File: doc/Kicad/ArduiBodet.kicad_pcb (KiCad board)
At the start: 2 copper layers, 80 x 49.5 mm, 15 parts, among them CON1 BARREL_JACK, IC1 ATMEGA328-P, IC2 SN754410, P1 ISP10PIN, P2 DS3231_Breakout_Connector, P3 Moteur Horloge, SW1 SWITCH_INV, SW2 Switch_DPST

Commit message: routing in progress
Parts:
- added C4: 1000 uF, Capacitors_Elko_ThroughHole:Elko_vert_20x10mm_RM2.5, F.Cu at (157.5, 95.2)
- added C5: 330nF, Capacitors_ThroughHole:C_Rect_L4_W2.5_P2.5, F.Cu at (167.6, 95.2)
- added U1: LM7805CT, Power_Integrations:TO-220, F.Cu at (146.1, 102.9)
- C2: value CP -> 100 nF; footprint Capacitors_Elko_ThroughHole:Elko_vert_20x10mm_RM2.5 -> Capacitors_ThroughHole:C_Rect_L4_W2.5_P2.5
- CON1: footprint Connect:BARREL_JACK -> myLib:BARREL_JACK_FR
- moved C2 50.8 mm to (143.5, 95.2), turned to 0 degrees
- moved C1 18.5 mm to (186.7, 113.0)
- moved SW1 15.9 mm to (177.8, 109.2)
- moved P2 14.9 mm to (129.5, 115.6)
- moved IC2 13.7 mm to (188.0, 128.3)
- moved R2 13.7 mm to (176.5, 132.1)
- moved IC1 13.7 mm to (160.0, 120.7)
- moved P3 13.7 mm to (171.4, 138.4)
- moved SW2 13.7 mm to (153.7, 134.6)
- moved C3 13.7 mm to (158.8, 129.5)
- moved R3 13.7 mm to (156.2, 144.8)
- moved D1 13.7 mm to (161.3, 139.7)
- moved P1 13.5 mm to (158.8, 105.4)
- moved R1 11.7 mm to (134.6, 119.4)
- moved CON1 2.84 mm to (190.5, 97.8)
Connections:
- CON1 pad 2: GNDA -> Net-(CON1-Pad2)
- CON1 pad 3: Net-(CON1-Pad3) -> GNDA
- IC2 pad 8: Net-(C1-Pad1) -> Net-(C4-Pad1)
- SW1 pad 1: Net-(C1-Pad1) -> Net-(SW1-Pad1)
- SW1 pad 3: Net-(SW1-Pad3) -> Net-(C4-Pad1)
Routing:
- net GNDA: track 0.00 -> 143.9 mm
- net Net-(C4-Pad1): track 0.00 -> 130.0 mm
- net Net-(C1-Pad1): track 0.00 -> 76.2 mm
- net Net-(IC2-Pad3): track 0.00 -> 62.8 mm
- net Net-(IC1-Pad1): track 0.00 -> 52.1 mm, vias 0 -> 2
- net Net-(IC1-Pad16): track 0.00 -> 27.5 mm
- net Net-(IC1-Pad4): track 0.00 -> 25.0 mm
- net Net-(IC1-Pad17): track 0.00 -> 24.1 mm, vias 0 -> 2
- net Net-(IC1-Pad27): track 0.00 -> 20.9 mm
- net Net-(IC1-Pad28): track 0.00 -> 16.6 mm
- net Net-(CON1-Pad1): track 0.00 -> 11.6 mm
- net Net-(IC1-Pad19): track 0.00 -> 11.4 mm
- net Net-(IC1-Pad18): track 0.00 -> 11.4 mm
- net Net-(IC1-Pad6): track 0.00 -> 11.2 mm
- net Net-(R3-Pad2): track 0.00 -> 7.62 mm
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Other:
- board size 80 x 49.5 mm -> 80 x 61 mm

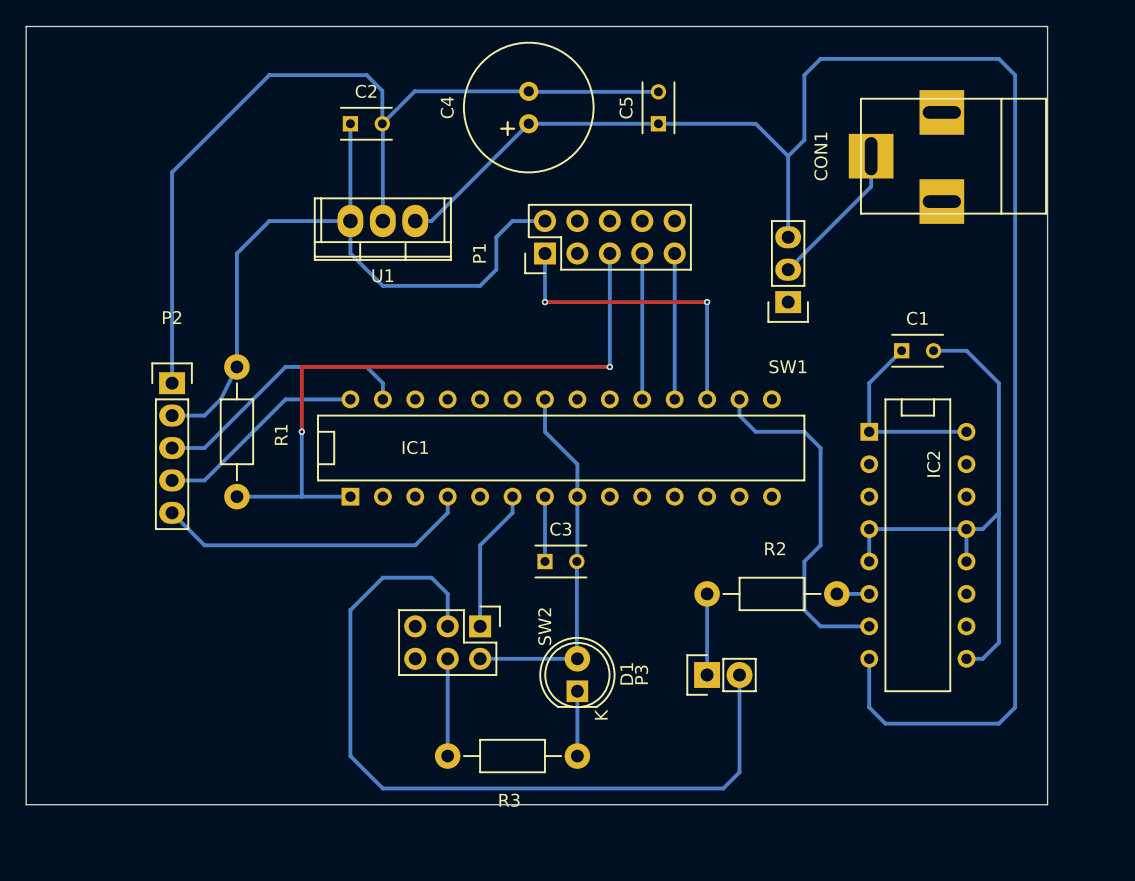
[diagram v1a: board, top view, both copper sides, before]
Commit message: fully routed #1 fixed custom BARREL_JACK_FR.kicad_mod
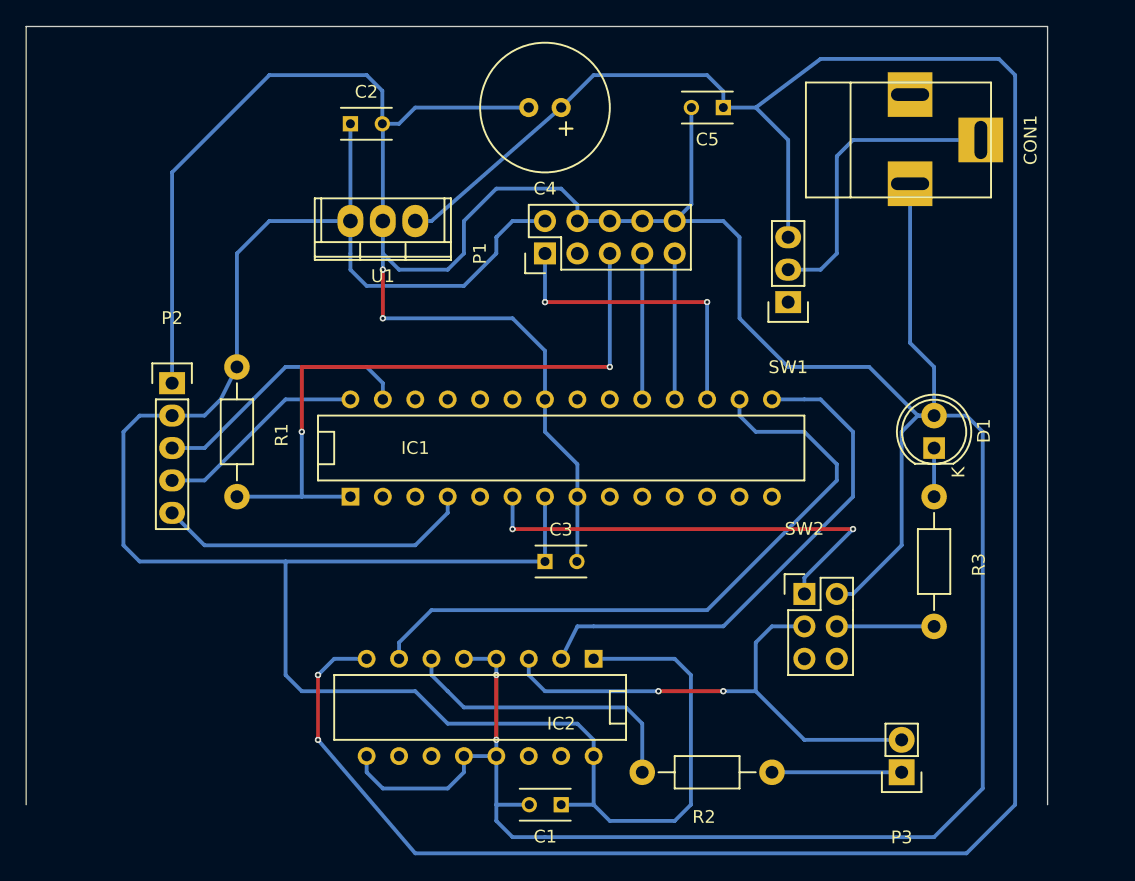
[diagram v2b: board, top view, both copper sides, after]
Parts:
- moved C1 44.4 mm to (160.0, 148.6), turned to 180 degrees
- moved IC2 36.6 mm to (153.7, 141.0), turned to 180 degrees
- moved R3 36.4 mm to (189.2, 129.5), turned to 270 degrees
- moved D1 33.8 mm to (189.2, 120.7)
- moved SW2 25.5 mm to (179.1, 132.1), turned to 0 degrees
- moved P3 17.0 mm to (186.7, 146.1), turned to 180 degrees
- moved R2 14.9 mm to (171.4, 146.1), turned to 180 degrees
- moved C5 5.24 mm to (172.7, 94.0), turned to 180 degrees
- moved CON1 4.02 mm to (186.7, 96.5), turned to 0 degrees
- moved C4 2.84 mm to (160.0, 94.0), turned to 180 degrees
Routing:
- net GNDA: track 143.9 -> 308.7 mm, vias 0 -> 4
- net Net-(C1-Pad1): track 76.2 -> 177.6 mm
- net Net-(C4-Pad1): track 130.0 -> 193.0 mm, vias 0 -> 2
- net Net-(IC1-Pad15): track 0.00 -> 41.1 mm
- net Net-(IC1-Pad16): track 27.5 -> 52.6 mm
- net Net-(IC1-Pad6): track 11.2 -> 35.9 mm, vias 0 -> 2
- net Net-(IC2-Pad3): track 62.8 -> 40.7 mm, vias 0 -> 2
- net Net-(IC2-Pad6): track 2.54 -> 23.2 mm
- net Net-(CON1-Pad1): track 11.6 -> 23.8 mm
- net Net-(P3-Pad1): track 6.35 -> 10.2 mm
- net Net-(D1-Pad1): track 5.08 -> 3.81 mm

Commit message: routing almost done
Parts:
- added REF**: MountingHole_3mm, Mounting_Holes:MountingHole_3mm, F.Cu at (133.3, 141.0)
- added REF**: MountingHole_3mm, Mounting_Holes:MountingHole_3mm, F.Cu at (193.0, 141.0)
- added REF**: MountingHole_3mm, Mounting_Holes:MountingHole_3mm, F.Cu at (191.8, 92.7)
- added REF**: MountingHole_3mm, Mounting_Holes:MountingHole_3mm, F.Cu at (133.3, 92.7)
- SW2: footprint Pin_Headers:Pin_Header_Straight_2x03 -> myLib:Pin_Header_Straight_2x03_for_SPDT_switch
- moved IC2 10.8 mm to (161.3, 133.3)
- moved C1 9.92 mm to (166.4, 141.0)
- moved P3 9.25 mm to (184.2, 137.2), turned to 270 degrees
- moved R2 9.16 mm to (179.1, 141.0)
- moved CON1 8.98 mm to (188.0, 105.4)
- moved SW2 8.98 mm to (185.4, 125.7)
- moved R3 6.84 mm to (191.8, 123.2)
- moved D1 6.35 mm to (193.0, 115.6)
- moved C3 3.81 mm to (158.8, 125.7)
- moved P2 3.59 mm to (132.1, 113.0)
- moved R1 2.84 mm to (135.9, 116.8)
- moved IC1 2.54 mm to (160.0, 118.1)
- moved U1 2.54 mm to (146.1, 100.3)
- moved SW1 1.80 mm to (176.5, 108.0)
- moved C2 1.27 mm to (143.5, 94.0)
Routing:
- net GNDA: track 308.7 -> 276.3 mm
- net Net-(C1-Pad1): track 177.6 -> 157.5 mm, vias 0 -> 4
- net Net-(C4-Pad1): track 193.0 -> 173.0 mm, vias 2 -> 0
- net Net-(IC1-Pad15): track 41.1 -> 29.1 mm
- net Net-(IC1-Pad16): track 52.6 -> 40.8 mm
- net Net-(IC1-Pad6): track 35.9 -> 43.2 mm
- net Net-(IC2-Pad3): track 40.7 -> 47.6 mm, vias 2 -> 0
- net Net-(IC2-Pad6): track 23.2 -> 29.8 mm
- net Net-(P3-Pad1): track 10.2 -> 3.81 mm
- net Net-(CON1-Pad1): track 23.8 -> 28.6 mm
- net Net-(R3-Pad2): track 7.62 -> 3.81 mm
- net Net-(IC1-Pad1): track 52.1 -> 48.3 mm
- net Net-(IC1-Pad4): track 25.0 -> 21.4 mm
- net Net-(IC1-Pad27): track 20.9 -> 18.4 mm
- net Net-(IC1-Pad28): track 16.6 -> 14.1 mm
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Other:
- board size 80 x 61 mm -> 69.8 x 58.4 mm
- net class Default: trace_width 0.3 -> 0.4; via_dia 0.5 -> 1.27; via_drill 0.3 -> 0.5
- net class GNDA added: clearance 0.3, trace_width 0.6, via_dia 1.27, via_drill 0.5
- net class Power added: clearance 0.3, trace_width 0.6, via_dia 1.27, via_drill 0.5
- board text added: "ArduiBodet V1.0 (c) Patrice Godard"

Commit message: routing in progress
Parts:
- removed REF** (x4): MountingHole_3mm, Mounting_Holes:MountingHole_3mm
- added ?: , myLib:MountingHole_1.5mm, F.Cu at (193.0, 94.0)
- added ?: , myLib:MountingHole_1.5mm, F.Cu at (194.3, 139.7)
- added ?: , myLib:MountingHole_1.5mm, F.Cu at (132.1, 94.0)
- added ?: , myLib:MountingHole_1.5mm, F.Cu at (142.5, 139.7)
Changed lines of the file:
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@@
     (links 52)
     (no_connects 0)
-    (area 128.219999 87.579999 198.170001 146.100001)
+    (area 121.014522 86.405 199.195 146.100001)
     (thickness 1.6)
     (drawings 6)
@@
       (net 2 GNDA))
   )
-  (module Mounting_Holes:MountingHole_3mm (layer F.Cu)
-    (at 133.35 140.97)
-    (descr "Mounting hole, Befestigungsbohrung, 3mm, No Annular, Kein Restring,")
-    (tags "Mounting hole, Befestigungsbohrung, 3mm, No Annular, Kein Restring,")
-    (fp_text reference REF** (at 0 -4.0005) (layer F.SilkS)
-      (effects (font (size 1 1) (thickness 0.15)))
-    )
-    (fp_text value MountingHole_3mm (at 1.00076 5.00126) (layer F.Fab)
-      (effects (font (size 1 1) (thickness 0.15)))
-    )
-    (fp_circle (center 0 0) (end 3 0) (layer Cmts.User) (width 0.381))
-    (pad 1 thru_hole circle (at 0 0) (size 3 3) (drill 3) (layers))
-  )
-  (module Mounting_Holes:MountingHole_3mm (layer F.Cu)
-    (at 193.04 140.97)
-    (descr "Mounting hole, Befestigungsbohrung, 3mm, No Annular, Kein Restring,")
-    (tags "Mounting hole, Befestigungsbohrung, 3mm, No Annular, Kein Restring,")
-    (fp_text reference REF** (at 0 -4.0005) (layer F.SilkS)
-      (effects (font (size 1 1) (thickness 0.15)))
-    )
-    (fp_text value MountingHole_3mm (at 1.00076 5.00126) (layer F.Fab)
-      (effects (font (size 1 1) (thickness 0.15)))
-    )
-    (fp_circle (center 0 0) (end 3 0) (layer Cmts.User) (width 0.381))
-    (pad 1 thru_hole circle (at 0 0) (size 3 3) (drill 3) (layers))
-  )
-  (module Mounting_Holes:MountingHole_3mm (layer F.Cu)
-    (at 191.77 92.71)
-    (descr "Mounting hole, Befestigungsbohrung, 3mm, No Annular, Kein Restring,")
-    (tags "Mounting hole, Befestigungsbohrung, 3mm, No Annular, Kein Restring,")
-    (fp_text reference REF** (at 0 -4.0005) (layer F.SilkS)
-      (effects (font (size 1 1) (thickness 0.15)))
-    )
-    (fp_text value MountingHole_3mm (at 1.00076 5.00126) (layer F.Fab)
-      (effects (font (size 1 1) (thickness 0.15)))
-    )
-    (fp_circle (center 0 0) (end 3 0) (layer Cmts.User) (width 0.381))
-    (pad 1 thru_hole circle (at 0 0) (size 3 3) (drill 3) (layers))
-  )
-  (module Mounting_Holes:MountingHole_3mm (layer F.Cu)
-    (at 133.35 92.71)
-    (descr "Mounting hole, Befestigungsbohrung, 3mm, No Annular, Kein Restring,")
-    (tags "Mounting hole, Befestigungsbohrung, 3mm, No Annular, Kein Restring,")
-    (fp_text reference REF** (at 0 -4.0005) (layer F.SilkS)
-      (effects (font (size 1 1) (thickness 0.15)))
-    )
-    (fp_text value MountingHole_3mm (at 1.00076 5.00126) (layer F.Fab)
-      (effects (font (size 1 1) (thickness 0.15)))
-    )
-    (fp_circle (center 0 0) (end 3 0) (layer Cmts.User) (width 0.381))
-    (pad 1 thru_hole circle (at 0 0) (size 3 3) (drill 3) (layers))
-  )
   (module myLib:Pin_Header_Straight_2x03_for_SPDT_switch (layer F.Cu)
     (at 185.42 125.73)
@@
     )
   )
-  (gr_text "ArduiBodet V1.0\n(c) Patrice Godard" (at 140.97 135.89 315) (layer B.Cu)
+  (module myLib:MountingHole_1.5mm (layer F.Cu)
+    (at 193.04 93.98)
+    (descr "Mounting hole, Befestigungsbohrung, 3mm, No Annular, Kein Restring,")
+    (tags "Mounting hole, Befestigungsbohrung, 3mm, No Annular, Kein Restring,")
+    (fp_text reference "" (at 0 -4.0005) (layer F.SilkS)
+      (effects (font (size 1 1) (thickness 0.15)))
+    )
+    (fp_text value "" (at 1.00076 5.00126) (layer F.Fab)
+      (effects (font (size 1 1) (thickness 0.15)))
+    )
+    (fp_circle (center 0 0) (end 1.5 0) (layer Cmts.User) (width 0.381))
+    (pad 1 thru_hole circle (at 0 0) (size 3 3) (drill 3) (layers))
+  )
+  (module myLib:MountingHole_1.5mm (layer F.Cu)
+    (at 194.31 139.7)
+    (descr "Mounting hole, Befestigungsbohrung, 3mm, No Annular, Kein Restring,")
+    (tags "Mounting hole, Befestigungsbohrung, 3mm, No Annular, Kein Restring,")
+    (fp_text reference "" (at 0 -4.0005) (layer F.SilkS)
+      (effects (font (size 1 1) (thickness 0.15)))
+    )
+    (fp_text value "" (at 1.00076 5.00126) (layer F.Fab)
+      (effects (font (size 1 1) (thickness 0.15)))
+    )
+    (fp_circle (center 0 0) (end 1.5 0) (layer Cmts.User) (width 0.381))
+    (pad 1 thru_hole circle (at 0 0) (size 3 3) (drill 3) (layers))
+  )
+  (module myLib:MountingHole_1.5mm (layer F.Cu)
+    (at 132.08 93.98)
+    (descr "Mounting hole, Befestigungsbohrung, 3mm, No Annular, Kein Restring,")
+    (tags "Mounting hole, Befestigungsbohrung, 3mm, No Annular, Kein Restring,")
+    (fp_text reference "" (at 0 -4.0005) (layer F.SilkS)
+      (effects (font (size 1 1) (thickness 0.15)))
+    )
+    (fp_text value "" (at 1.00076 5.00126) (layer F.Fab)
+      (effects (font (size 1 1) (thickness 0.15)))
+    )
+    (fp_circle (center 0 0) (end 1.5 0) (layer Cmts.User) (width 0.381))
+    (pad 1 thru_hole circle (at 0 0) (size 3 3) (drill 3) (layers))
+  )
+  (module myLib:MountingHole_1.5mm (layer F.Cu)
+    (at 142.494 139.7)
+    (descr "Mounting hole, Befestigungsbohrung, 3mm, No Annular, Kein Restring,")
+    (tags "Mounting hole, Befestigungsbohrung, 3mm, No Annular, Kein Restring,")
+    (fp_text reference "" (at 0 -4.0005) (layer F.SilkS)
+      (effects (font (size 1 1) (thickness 0.15)))
+    )
+    (fp_text value "" (at 1.00076 5.00126) (layer F.Fab)
+      (effects (font (size 1 1) (thickness 0.15)))
+    )
+    (fp_circle (center 0 0) (end 1.5 0) (layer Cmts.User) (width 0.381))
+    (pad 1 thru_hole circle (at 0 0) (size 3 3) (drill 3) (layers))
+  )
+  (gr_text "ArduiBodet V1.0\n(c) Patrice Godard" (at 139.192 129.032) (layer B.Cu)
     (effects (font (size 1.5 1.5) (thickness 0.3)) (justify mirror))
   )
@@
   (segment (start 182.88 120.65) (end 173.99 129.54) (width 0.4) (layer B.Cu) (net 1))
   (segment (start 158.75 121.92) (end 158.75 119.38) (width 0.4) (layer B.Cu) (net 1))
-  (segment (start 185.42 128.27) (end 184.15 128.27) (width 0.6) (layer B.Cu) (net 2) (status 400000))
+  (segment (start 185.42 128.27) (end 184.15 128.27) (width 0.6) (layer B.Cu) (net 2))
   (segment (start 184.15 121.92) (end 184.15 111.76) (width 0.6) (layer B.Cu) (net 2))
   (segment (start 182.88 123.19) (end 184.15 121.92) (width 0.6) (layer B.Cu) (net 2))
@@
   (segment (start 132.08 120.65) (end 132.08 120.65) (width 0.4) (layer B.Cu) (net 29) (status 20))
   (segment (start 138.43 114.3) (end 132.08 120.65) (width 0.4) (layer B.Cu) (net 29))
-  (segment (start 187.96 125.73) (end 193.04 125.73) (width 0.6) (layer B.Cu) (net 30) (status 400000))
+  (segment (start 187.96 125.73) (end 193.04 125.73) (width 0.6) (layer B.Cu) (net 30))
   (segment (start 182.88 133.35) (end 181.61 134.62) (width 0.6) (layer B.Cu) (net 30))
   (segment (start 193.04 133.35) (end 182.88 133.35) (width 0.6) (layer B.Cu) (net 30))
@@
   (segment (start 157.48 129.54) (end 157.48 130.81) (width 0.6) (layer B.Cu) (net 31) (status 10))
   (segment (start 184.15 137.16) (end 184.15 140.97) (width 0.6) (layer B.Cu) (net 37))
-  (segment (start 191.77 128.27) (end 187.96 128.27) (width 0.4) (layer B.Cu) (net 38) (status C00000))
+  (segment (start 191.77 128.27) (end 187.96 128.27) (width 0.4) (layer B.Cu) (net 38))
   (segment (start 151.13 96.52) (end 148.59 100.33) (width 0.6) (layer B.Cu) (net 39))
   (segment (start 158.75 96.52) (end 151.13 96.52) (width 0.6) (layer B.Cu) (net 39) (status 10))

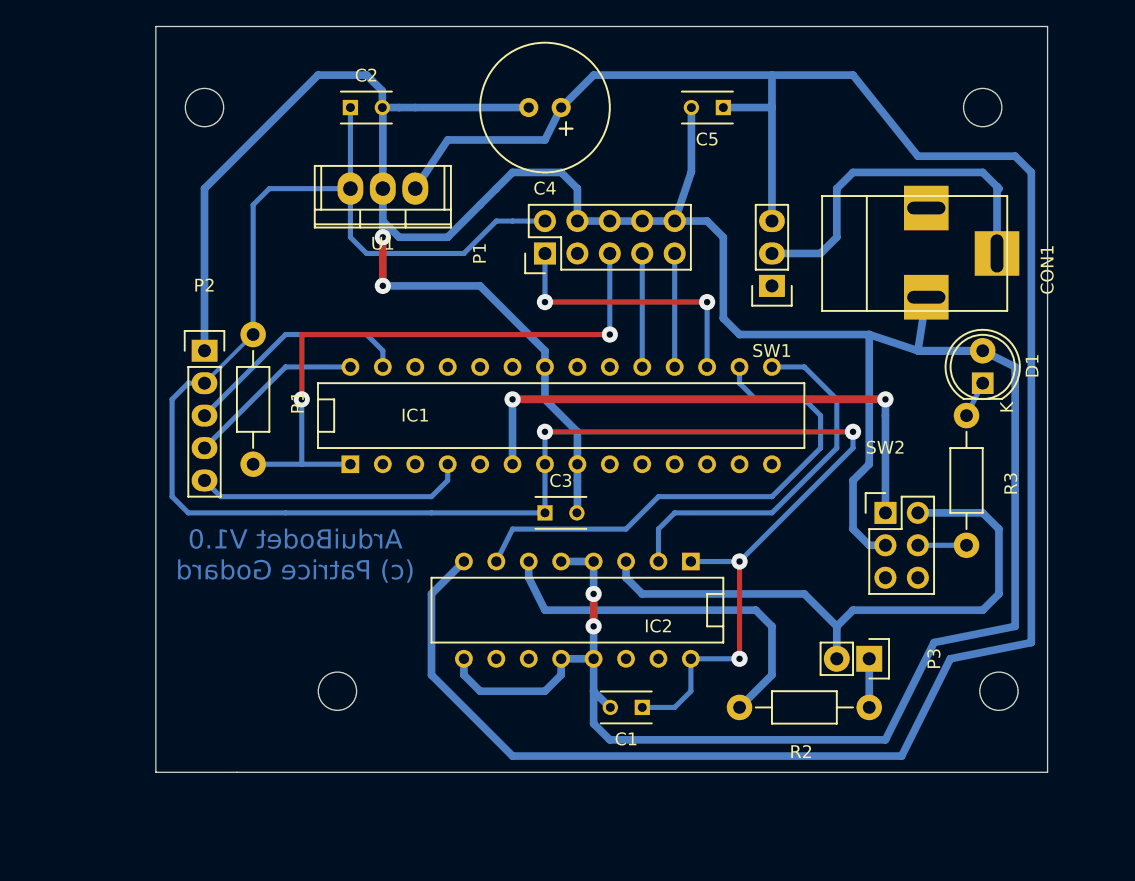
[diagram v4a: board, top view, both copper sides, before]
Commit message: routing done. needs proof-checking
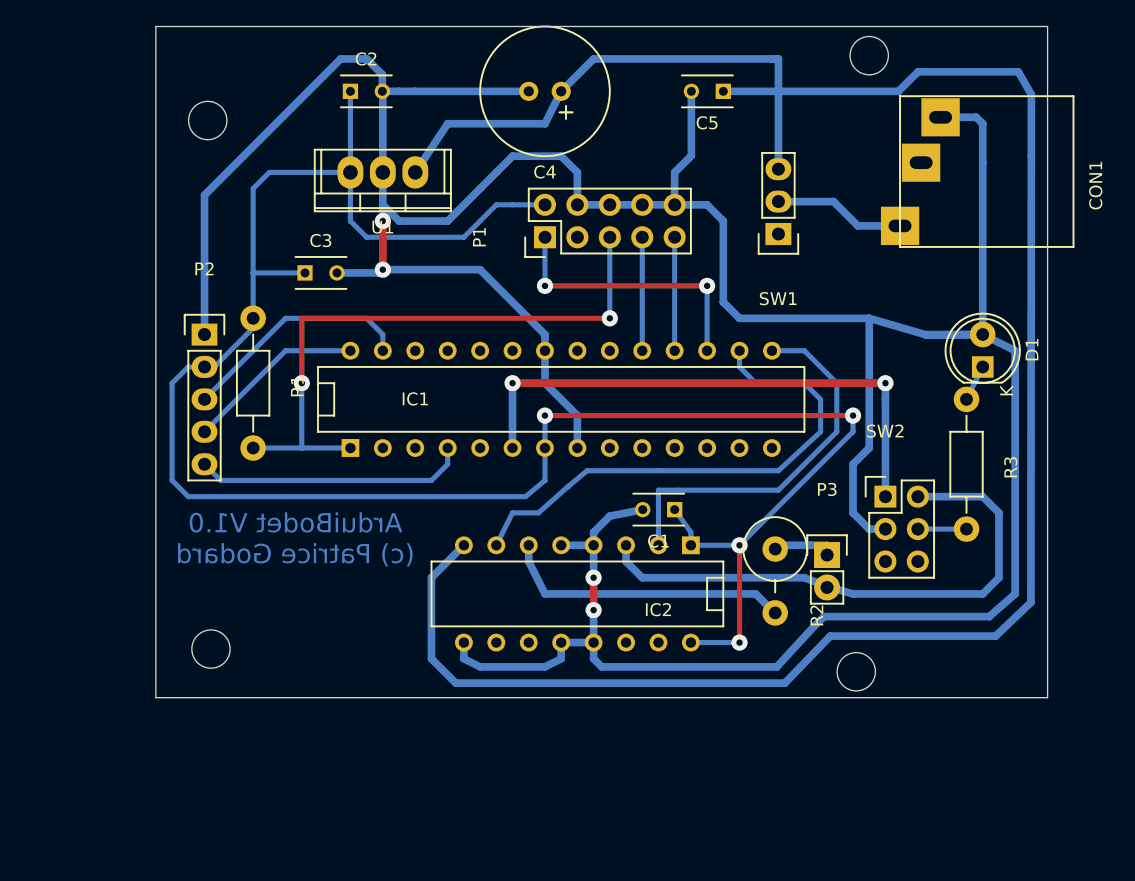
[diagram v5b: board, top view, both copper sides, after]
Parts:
- R2: footprint Resistors_ThroughHole:Resistor_Horizontal_RM10mm -> Resistors_ThroughHole:Resistor_Vertical_RM5mm
- moved C3 26.6 mm to (140.0, 106.9)
- moved C1 15.7 mm to (168.9, 125.5)
- moved ? 11.3 mm to (183.1, 138.2)
- moved ? 10.4 mm to (132.6, 136.4)
- moved R2 10.2 mm to (176.8, 131.1), turned to 270 degrees
- moved ? 9.77 mm to (184.2, 89.9)
- moved P3 8.77 mm to (180.8, 129.0), turned to 0 degrees
- moved CON1 7.62 mm to (191.8, 98.8)
- moved SW1 4.10 mm to (177.0, 103.9)
- moved C2 1.27 mm to (143.5, 92.7)
- moved C4 1.27 mm to (160.0, 92.7)
- moved C5 1.27 mm to (172.7, 92.7)
- moved R1 1.27 mm to (135.9, 115.6)
- moved SW2 1.27 mm to (185.4, 124.5)
- moved D1 1.27 mm to (193.0, 114.3)
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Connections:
- CON1 pad 2: Net-(CON1-Pad2) -> GNDA
- CON1 pad 3: GNDA -> Net-(CON1-Pad3)
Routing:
- net Net-(CON1-Pad1): track 28.6 -> 10.3 mm
- net GNDA: track 276.3 -> 285.6 mm
- net Net-(IC2-Pad6): track 29.8 -> 22.4 mm
- net Net-(C4-Pad1): track 173.0 -> 167.6 mm
- net Net-(IC2-Pad3): track 47.6 -> 44.0 mm
- net Net-(IC1-Pad15): track 29.1 -> 30.1 mm
- net Net-(P3-Pad1): track 3.81 -> 4.57 mm
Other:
- board size 69.8 x 58.4 mm -> 69.8 x 52.6 mm
